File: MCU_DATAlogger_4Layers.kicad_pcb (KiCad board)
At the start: 4 copper layers, 51.5 x 35.7 mm, 30 parts, among them J1 Conn_01x04_Pin, J2 Conn_01x04_Pin, J3 Conn_01x09_Pin, J4 Conn_02x03_Odd_Even, U1 24LC1025, U2 24LC1025, U3 ATMEGA328P-AU, U4 DS1337S_, Y1 32.768KHz, Y2 16MHz

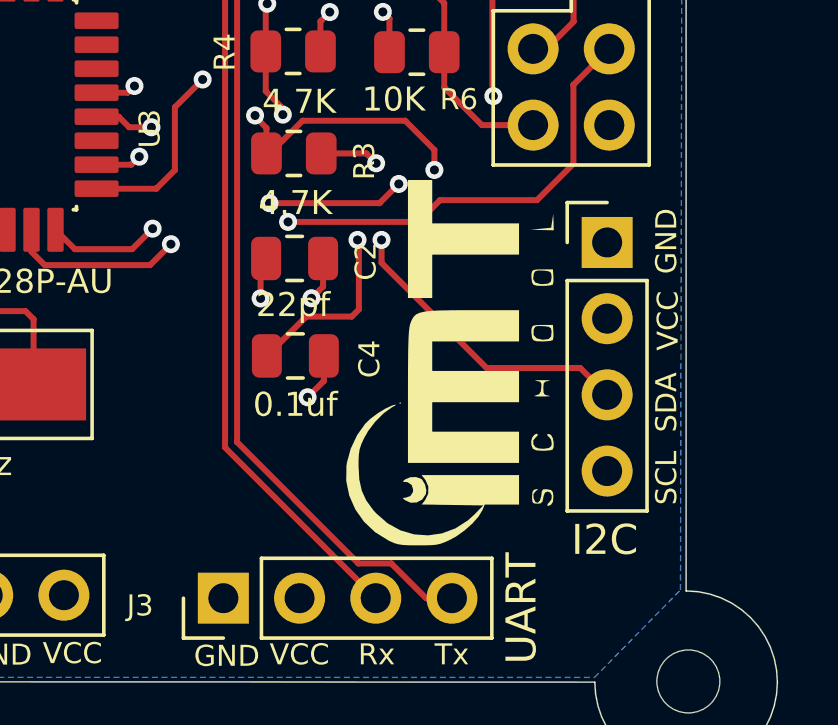
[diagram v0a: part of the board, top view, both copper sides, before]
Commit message: Added new IMT Logo on the layout design
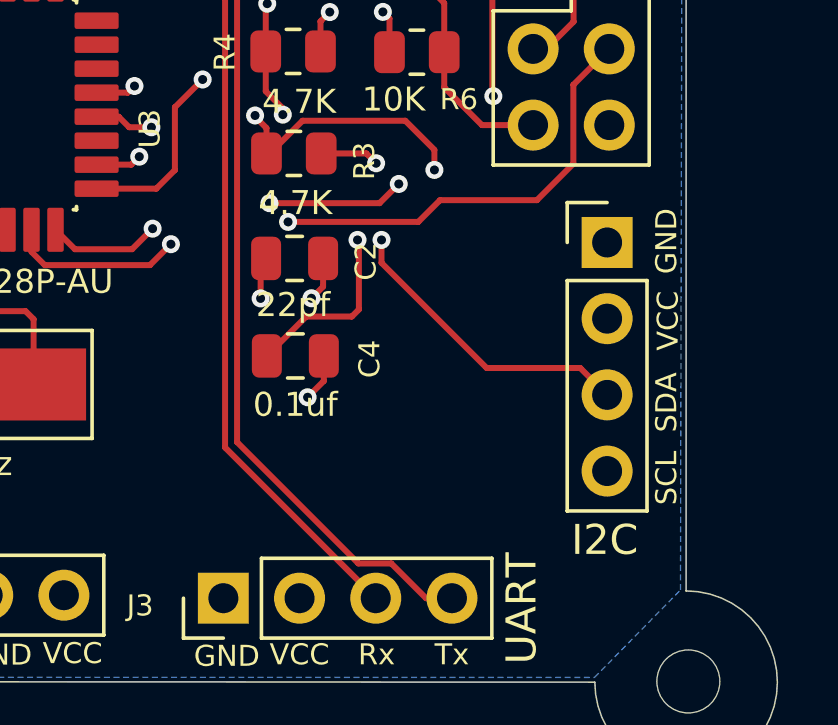
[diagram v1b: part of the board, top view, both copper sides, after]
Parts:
- removed the G*** at (154.3, 96.2)
- added G***: LOGO, logo_Footprints:imt_new3, B.Cu at (139.6, 96.3)
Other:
- board text removed: "IMT SCHOOL"
